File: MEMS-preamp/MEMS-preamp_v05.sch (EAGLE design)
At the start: 20 parts

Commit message: new mems preamp added
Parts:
- removed R2, R4: 200K, adafruit:TRIMPOT3386
- added POT1: POT-DUAL-PTV112-4420, CMU-ArtFab:POT-DUAL-PTV112-4420
- R1, R3: value 1K -> 220
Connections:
- net GROU[: now also POT1/2.E; no longer R4.A
- net N$10: now also POT1/2.A; no longer R4.S
- net N$5: now also POT1/1.E; no longer R2.A
- net N$9: now also POT1/1.A; no longer R2.S
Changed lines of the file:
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@@
 <layer number="132" name="bAdjust" color="7" fill="1" visible="yes" active="yes"/>
 <layer number="144" name="Drill_legend" color="7" fill="1" visible="yes" active="yes"/>
+<layer number="145" name="DrillLegend_01-16" color="7" fill="1" visible="yes" active="yes"/>
+<layer number="146" name="DrillLegend_01-20" color="7" fill="1" visible="yes" active="yes"/>
 <layer number="150" name="Notes" color="7" fill="1" visible="yes" active="yes"/>
 <layer number="151" name="HeatSink" color="7" fill="1" visible="yes" active="yes"/>
@@
 <attribute name="CON5" value="DC"/>
 </part>
-<part name="R1" library="CMU-ArtFab" deviceset="R-US_" device="0204/5" value="1K"/>
+<part name="R1" library="CMU-ArtFab" deviceset="R-US_" device="0204/5" value="220"/>
 <part name="GND2" library="supply1" deviceset="GND" device=""/>
 <part name="R9" library="CMU-ArtFab" deviceset="R-US_" device="0204/5" value="10"/>
@@
 <part name="GND1" library="supply1" deviceset="GND" device=""/>
 <part name="R10" library="CMU-ArtFab" deviceset="R-US_" device="0204/5" value="390"/>
-<part name="R2" library="adafruit" deviceset="TRIMPOT" device="3386" value="200K"/>
 <part name="J_REG_12V" library="CMU-ArtFab" deviceset="POLOLU_VOLTAGE_REGULATORS_3PIN" device="" value="POLOLU_VOLTAGE_REGULATORS_3PIN"/>
 <part name="GND12" library="supply1" deviceset="GND" device=""/>
@@
 <part name="P+2" library="supply1" deviceset="+12V" device=""/>
 <part name="BATTERY" library="SparkFun-Connectors" deviceset="CONN_02" device="LOCK"/>
-<part name="R3" library="CMU-ArtFab" deviceset="R-US_" device="0204/5" value="1K"/>
-<part name="R4" library="adafruit" deviceset="TRIMPOT" device="3386" value="200K"/>
+<part name="R3" library="CMU-ArtFab" deviceset="R-US_" device="0204/5" value="220"/>
 <part name="C2" library="rcl" deviceset="CPOL-EU" device="E2.5-5" value="10u"/>
+<part name="POT1" library="CMU-ArtFab" deviceset="POT-DUAL-PTV112" device="-4420"/>
 </parts>
 <sheets>
@@
 </instance>
 <instance part="R10" gate="G$1" x="142.24" y="162.56" rot="R90"/>
-<instance part="R2" gate="G$1" x="78.74" y="50.8" rot="R270"/>
 <instance part="J_REG_12V" gate="J_REG_5V" x="76.2" y="165.1"/>
 <instance part="GND12" gate="1" x="76.2" y="144.78" smashed="yes">
@@
 <instance part="BATTERY" gate="G$1" x="30.48" y="162.56" rot="R180"/>
 <instance part="R3" gate="G$1" x="119.38" y="71.12"/>
-<instance part="R4" gate="G$1" x="144.78" y="50.8" rot="R270"/>
 <instance part="C2" gate="G$1" x="165.1" y="71.12" smashed="yes" rot="R90">
 <attribute name="NAME" x="163.703" y="74.1426" size="1.778" layer="95" ratio="12"/>
 <attribute name="VALUE" x="163.703" y="66.5226" size="1.778" layer="96" ratio="12"/>
 </instance>
+<instance part="POT1" gate="/1" x="81.28" y="50.8" rot="R90"/>
+<instance part="POT1" gate="/2" x="147.32" y="53.34" rot="R90"/>
 </instances>
 <busses>
@@
 <wire x1="53.34" y1="50.8" x2="53.34" y2="68.58" width="0.1524" layer="91"/>
 <junction x="53.34" y="68.58"/>
-<pinref part="R2" gate="G$1" pin="A"/>
+<pinref part="POT1" gate="/1" pin="E"/>
 </segment>
 </net>
@@
 <pinref part="C1" gate="G$1" pin="+"/>
 <wire x1="76.2" y1="71.12" x2="88.9" y2="71.12" width="0.1524" layer="91"/>
-<pinref part="R2" gate="G$1" pin="S"/>
+<pinref part="POT1" gate="/1" pin="A"/>
 <wire x1="88.9" y1="71.12" x2="96.52" y2="71.12" width="0.1524" layer="91"/>
-<wire x1="78.74" y1="45.72" x2="78.74" y2="40.64" width="0.1524" layer="91"/>
-<wire x1="78.74" y1="40.64" x2="88.9" y2="40.64" width="0.1524" layer="91"/>
-<wire x1="88.9" y1="40.64" x2="88.9" y2="71.12" width="0.1524" layer="91"/>
+<wire x1="88.9" y1="50.8" x2="88.9" y2="71.12" width="0.1524" layer="91"/>
 <junction x="88.9" y="71.12"/>
 </segment>
@@
 <segment>
 <pinref part="OPA2134" gate="B" pin="OUT"/>
-<wire x1="152.4" y1="71.12" x2="154.94" y2="71.12" width="0.1524" layer="91"/>
-<wire x1="154.94" y1="71.12" x2="154.94" y2="40.64" width="0.1524" layer="91"/>
-<wire x1="154.94" y1="40.64" x2="144.78" y2="40.64" width="0.1524" layer="91"/>
-<pinref part="R4" gate="G$1" pin="S"/>
-<wire x1="144.78" y1="40.64" x2="144.78" y2="45.72" width="0.1524" layer="91"/>
 <pinref part="C2" gate="G$1" pin="+"/>
 <wire x1="162.56" y1="71.12" x2="154.94" y2="71.12" width="0.1524" layer="91"/>
+<pinref part="POT1" gate="/2" pin="A"/>
+<wire x1="154.94" y1="71.12" x2="152.4" y2="71.12" width="0.1524" layer="91"/>
+<wire x1="154.94" y1="53.34" x2="154.94" y2="71.12" width="0.1524" layer="91"/>
 <junction x="154.94" y="71.12"/>
 </segment>
@@
 <pinref part="OPA2134" gate="B" pin="-IN"/>
 <wire x1="129.54" y1="68.58" x2="134.62" y2="68.58" width="0.1524" layer="91"/>
-<pinref part="R4" gate="G$1" pin="A"/>
 <wire x1="134.62" y1="68.58" x2="137.16" y2="68.58" width="0.1524" layer="91"/>
-<wire x1="139.7" y1="50.8" x2="139.7" y2="53.34" width="0.1524" layer="91"/>
 <wire x1="139.7" y1="53.34" x2="134.62" y2="53.34" width="0.1524" layer="91"/>
 <wire x1="134.62" y1="53.34" x2="134.62" y2="68.58" width="0.1524" layer="91"/>
 <junction x="134.62" y="68.58"/>
-</segment>
-</net>
+<pinref part="POT1" gate="/2" pin="E"/>
+</segment>
+</net>

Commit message: new mems preamp added
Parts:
- POT1: value POT-DUAL-PTV112-4420 -> 50k
- R1, R3: value 220 -> 1k
- R7, R8: value 47K -> 150k
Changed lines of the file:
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@@
 <part name="GND8" library="supply1" deviceset="GND" device=""/>
 <part name="GND4" library="supply1" deviceset="GND" device=""/>
-<part name="R7" library="CMU-ArtFab" deviceset="R-US_" device="0204/5" value="47K"/>
+<part name="R7" library="CMU-ArtFab" deviceset="R-US_" device="0204/5" value="150k"/>
 <part name="OPA2134" library="linear" deviceset="OPA2*" device="PA" technology="134" value="OPA2134PA">
 <attribute name="IC_NAME" value="TL072"/>
@@
 <attribute name="CON5" value="DC"/>
 </part>
-<part name="R1" library="CMU-ArtFab" deviceset="R-US_" device="0204/5" value="220"/>
+<part name="R1" library="CMU-ArtFab" deviceset="R-US_" device="0204/5" value="1k"/>
 <part name="GND2" library="supply1" deviceset="GND" device=""/>
 <part name="R9" library="CMU-ArtFab" deviceset="R-US_" device="0204/5" value="10"/>
 <part name="C4" library="rcl" deviceset="CPOL-EU" device="E2.5-5" value="100u"/>
-<part name="R8" library="CMU-ArtFab" deviceset="R-US_" device="0204/5" value="47K"/>
+<part name="R8" library="CMU-ArtFab" deviceset="R-US_" device="0204/5" value="150k"/>
 <part name="U$1" library="CMU-ArtFab" deviceset="1/8&quot;-F-STEREO-PCB" device=""/>
 <part name="GND10" library="supply1" deviceset="GND" device=""/>
@@
 <part name="P+2" library="supply1" deviceset="+12V" device=""/>
 <part name="BATTERY" library="SparkFun-Connectors" deviceset="CONN_02" device="LOCK"/>
-<part name="R3" library="CMU-ArtFab" deviceset="R-US_" device="0204/5" value="220"/>
+<part name="R3" library="CMU-ArtFab" deviceset="R-US_" device="0204/5" value="1k"/>
 <part name="C2" library="rcl" deviceset="CPOL-EU" device="E2.5-5" value="10u"/>
-<part name="POT1" library="CMU-ArtFab" deviceset="POT-DUAL-PTV112" device="-4420"/>
+<part name="POT1" library="CMU-ArtFab" deviceset="POT-DUAL-PTV112" device="-4420" value="50k"/>
 </parts>
 <sheets>

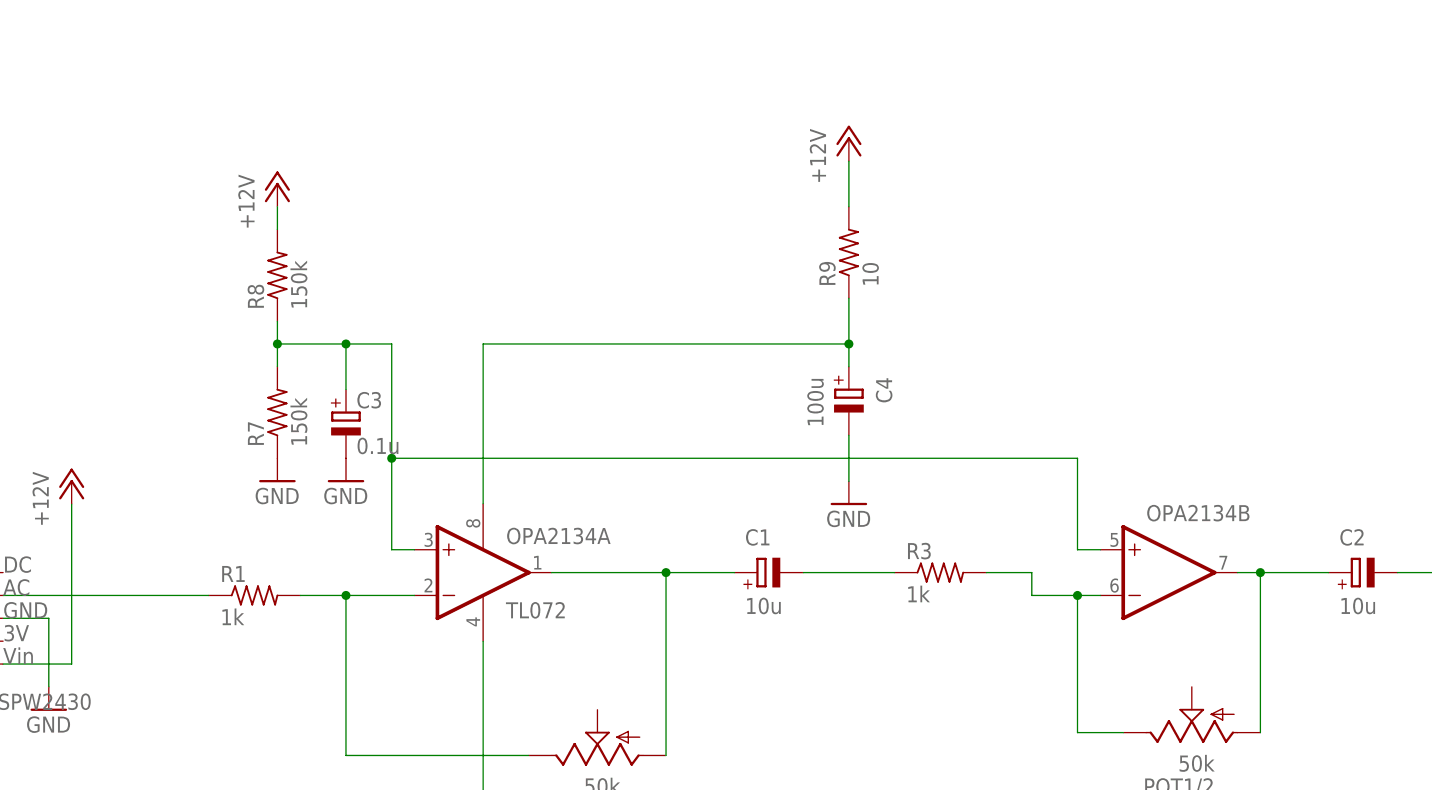
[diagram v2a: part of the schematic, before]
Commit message: new design for piezo premamp piezo-preamp-tickler_V3-2_single-supply-OPA1642 added
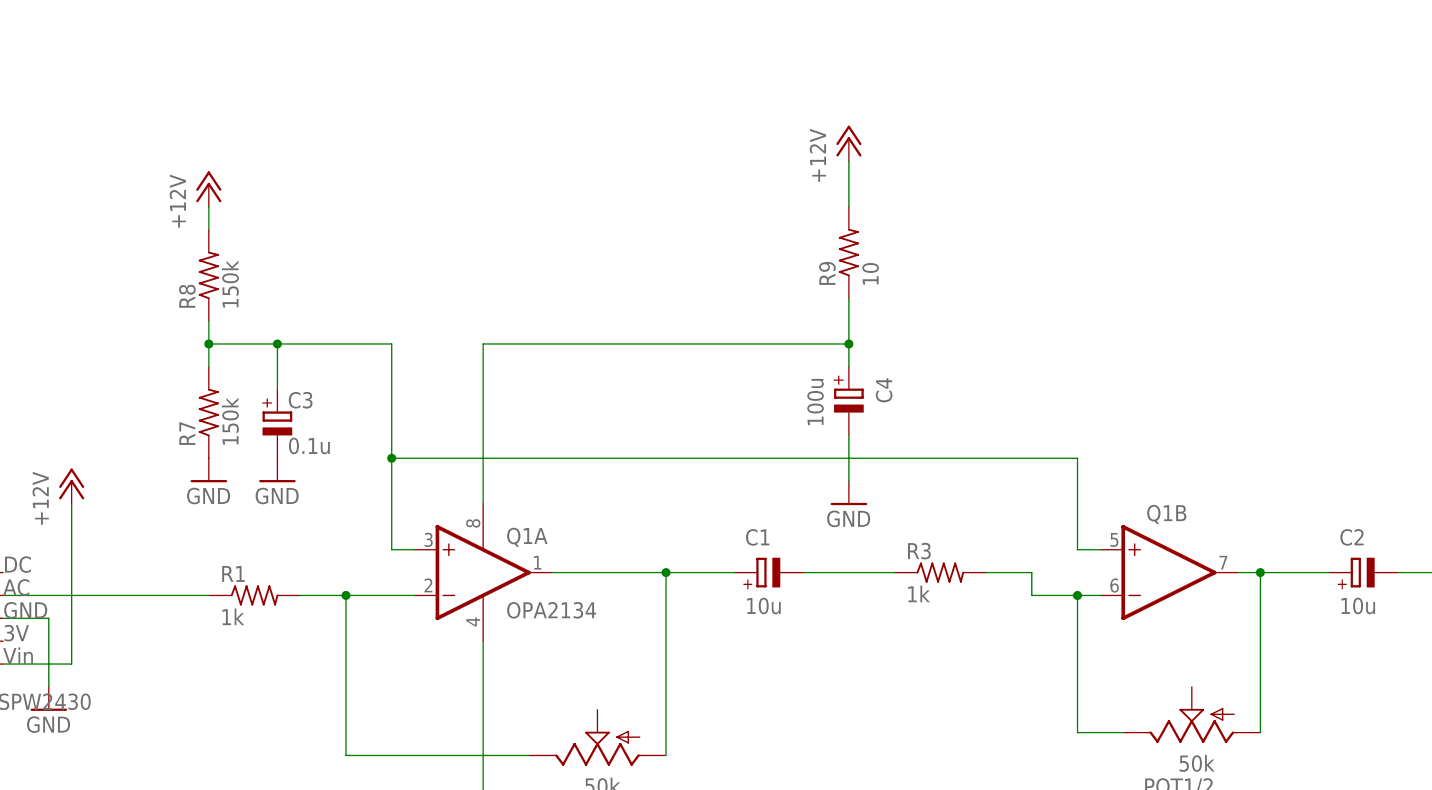
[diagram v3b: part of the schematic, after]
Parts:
- Q1: value OPA2134PA -> OPA2134; IC_NAME TL072 -> OPA2134
- renumbered OPA2134 to Q1
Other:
- moved on the sheet: C3, R7, R8
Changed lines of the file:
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@@
 <part name="GND4" library="supply1" deviceset="GND" device=""/>
 <part name="R7" library="CMU-ArtFab" deviceset="R-US_" device="0204/5" value="150k"/>
-<part name="OPA2134" library="linear" deviceset="OPA2*" device="PA" technology="134" value="OPA2134PA">
-<attribute name="IC_NAME" value="TL072"/>
+<part name="Q1" library="linear" deviceset="OPA2*" device="PA" technology="134" value="OPA2134">
+<attribute name="IC_NAME" value="OPA2134"/>
 </part>
 <part name="JP1" library="SparkFun-Connectors" deviceset="M05" device="LOCK" value="Adafruit-SPW2430">
@@
 </plain>
 <instances>
-<instance part="C3" gate="G$1" x="53.34" y="88.9" smashed="yes">
-<attribute name="NAME" x="54.483" y="89.3826" size="1.778" layer="95" ratio="12"/>
-<attribute name="VALUE" x="54.483" y="84.3026" size="1.778" layer="96" ratio="12"/>
+<instance part="C3" gate="G$1" x="45.72" y="88.9" smashed="yes">
+<attribute name="NAME" x="46.863" y="89.3826" size="1.778" layer="95" ratio="12"/>
+<attribute name="VALUE" x="46.863" y="84.3026" size="1.778" layer="96" ratio="12"/>
 </instance>
 <instance part="C1" gate="G$1" x="99.06" y="71.12" smashed="yes" rot="R90">
@@
 <attribute name="VALUE" x="97.663" y="66.5226" size="1.778" layer="96" ratio="12"/>
 </instance>
-<instance part="GND3" gate="1" x="45.72" y="81.28" smashed="yes">
+<instance part="GND3" gate="1" x="38.1" y="81.28" smashed="yes">
+<attribute name="VALUE" x="35.56" y="78.74" size="1.778" layer="96" ratio="12"/>
+</instance>
+<instance part="GND5" gate="1" x="45.72" y="81.28" smashed="yes">
 <attribute name="VALUE" x="43.18" y="78.74" size="1.778" layer="96" ratio="12"/>
-</instance>
-<instance part="GND5" gate="1" x="53.34" y="81.28" smashed="yes">
-<attribute name="VALUE" x="50.8" y="78.74" size="1.778" layer="96" ratio="12"/>
 </instance>
 <instance part="GND8" gate="1" x="109.22" y="78.74" smashed="yes">
@@
 <attribute name="VALUE" x="66.04" y="40.64" size="1.778" layer="96" ratio="12"/>
 </instance>
-<instance part="R7" gate="G$1" x="45.72" y="88.9" rot="R90"/>
-<instance part="OPA2134" gate="A" x="68.58" y="71.12" smashed="yes">
+<instance part="R7" gate="G$1" x="38.1" y="88.9" rot="R90"/>
+<instance part="Q1" gate="A" x="68.58" y="71.12" smashed="yes">
 <attribute name="NAME" x="71.12" y="74.295" size="1.778" layer="95"/>
 <attribute name="IC_NAME" x="71.12" y="66.04" size="1.778" layer="96"/>
 </instance>
-<instance part="OPA2134" gate="B" x="144.78" y="71.12" smashed="yes">
+<instance part="Q1" gate="B" x="144.78" y="71.12" smashed="yes">
 <attribute name="NAME" x="142.24" y="76.835" size="1.778" layer="95"/>
 </instance>
@@
 <attribute name="VALUE" x="104.6226" y="92.837" size="1.778" layer="96" ratio="12" rot="R270"/>
 </instance>
-<instance part="R8" gate="G$1" x="45.72" y="104.14" rot="R90"/>
+<instance part="R8" gate="G$1" x="38.1" y="104.14" rot="R90"/>
 <instance part="U$1" gate="G$1" x="195.58" y="63.5"/>
 <instance part="GND10" gate="1" x="185.42" y="60.96" smashed="yes">
@@
 <attribute name="VALUE" x="2.54" y="147.32" size="1.778" layer="96" ratio="12"/>
 </instance>
-<instance part="P+6" gate="1" x="45.72" y="114.3"/>
+<instance part="P+6" gate="1" x="38.1" y="114.3"/>
 <instance part="POWER" gate="G$1" x="12.7" y="157.48"/>
 <instance part="P+2" gate="1" x="22.86" y="81.28"/>
@@
 <pinref part="GND4" gate="1" pin="GND"/>
 <wire x1="68.58" y1="45.72" x2="68.58" y2="63.5" width="0.1524" layer="91"/>
-<pinref part="OPA2134" gate="A" pin="V-"/>
+<pinref part="Q1" gate="A" pin="V-"/>
 </segment>
 <segment>
@@
 <net name="N$8" class="0">
 <segment>
-<wire x1="53.34" y1="96.52" x2="53.34" y2="91.44" width="0.1524" layer="91"/>
+<wire x1="45.72" y1="96.52" x2="45.72" y2="91.44" width="0.1524" layer="91"/>
 <pinref part="C3" gate="G$1" pin="+"/>
-<wire x1="53.34" y1="96.52" x2="58.42" y2="96.52" width="0.1524" layer="91"/>
+<wire x1="45.72" y1="96.52" x2="58.42" y2="96.52" width="0.1524" layer="91"/>
 <wire x1="58.42" y1="96.52" x2="58.42" y2="83.82" width="0.1524" layer="91"/>
-<pinref part="OPA2134" gate="A" pin="+IN"/>
+<pinref part="Q1" gate="A" pin="+IN"/>
 <wire x1="58.42" y1="83.82" x2="58.42" y2="73.66" width="0.1524" layer="91"/>
 <wire x1="58.42" y1="73.66" x2="60.96" y2="73.66" width="0.1524" layer="91"/>
 <pinref part="R7" gate="G$1" pin="2"/>
 <pinref part="R8" gate="G$1" pin="1"/>
-<wire x1="45.72" y1="99.06" x2="45.72" y2="96.52" width="0.1524" layer="91"/>
-<wire x1="45.72" y1="96.52" x2="45.72" y2="93.98" width="0.1524" layer="91"/>
-<wire x1="53.34" y1="96.52" x2="45.72" y2="96.52" width="0.1524" layer="91"/>
-<junction x="53.34" y="96.52"/>
+<wire x1="38.1" y1="99.06" x2="38.1" y2="96.52" width="0.1524" layer="91"/>
+<wire x1="38.1" y1="96.52" x2="38.1" y2="93.98" width="0.1524" layer="91"/>
+<wire x1="45.72" y1="96.52" x2="38.1" y2="96.52" width="0.1524" layer="91"/>
 <junction x="45.72" y="96.52"/>
-<pinref part="OPA2134" gate="B" pin="+IN"/>
+<junction x="38.1" y="96.52"/>
+<pinref part="Q1" gate="B" pin="+IN"/>
 <wire x1="137.16" y1="73.66" x2="134.62" y2="73.66" width="0.1524" layer="91"/>
 <wire x1="134.62" y1="73.66" x2="134.62" y2="83.82" width="0.1524" layer="91"/>
@@
 <wire x1="53.34" y1="50.8" x2="73.66" y2="50.8" width="0.1524" layer="91"/>
 <pinref part="R1" gate="G$1" pin="2"/>
-<pinref part="OPA2134" gate="A" pin="-IN"/>
+<pinref part="Q1" gate="A" pin="-IN"/>
 <wire x1="48.26" y1="68.58" x2="53.34" y2="68.58" width="0.1524" layer="91"/>
 <wire x1="53.34" y1="68.58" x2="60.96" y2="68.58" width="0.1524" layer="91"/>
@@
 <net name="N$9" class="0">
 <segment>
-<pinref part="OPA2134" gate="A" pin="OUT"/>
+<pinref part="Q1" gate="A" pin="OUT"/>
 <pinref part="C1" gate="G$1" pin="+"/>
 <wire x1="76.2" y1="71.12" x2="88.9" y2="71.12" width="0.1524" layer="91"/>
@@
 <pinref part="R9" gate="G$1" pin="1"/>
 <wire x1="109.22" y1="101.6" x2="109.22" y2="96.52" width="0.1524" layer="91"/>
-<pinref part="OPA2134" gate="A" pin="V+"/>
+<pinref part="Q1" gate="A" pin="V+"/>
 <wire x1="109.22" y1="96.52" x2="109.22" y2="93.98" width="0.1524" layer="91"/>
 <wire x1="109.22" y1="96.52" x2="68.58" y2="96.52" width="0.1524" layer="91"/>
@@
 <segment>
 <pinref part="R8" gate="G$1" pin="2"/>
-<wire x1="45.72" y1="111.76" x2="45.72" y2="109.22" width="0.1524" layer="91"/>
+<wire x1="38.1" y1="111.76" x2="38.1" y2="109.22" width="0.1524" layer="91"/>
 <pinref part="P+6" gate="1" pin="+12V"/>
 </segment>
@@
 <net name="N$10" class="0">
 <segment>
-<pinref part="OPA2134" gate="B" pin="OUT"/>
+<pinref part="Q1" gate="B" pin="OUT"/>
 <pinref part="C2" gate="G$1" pin="+"/>
 <wire x1="162.56" y1="71.12" x2="154.94" y2="71.12" width="0.1524" layer="91"/>
@@
 <wire x1="124.46" y1="71.12" x2="129.54" y2="71.12" width="0.1524" layer="91"/>
 <wire x1="129.54" y1="71.12" x2="129.54" y2="68.58" width="0.1524" layer="91"/>
-<pinref part="OPA2134" gate="B" pin="-IN"/>
+<pinref part="Q1" gate="B" pin="-IN"/>
 <wire x1="129.54" y1="68.58" x2="134.62" y2="68.58" width="0.1524" layer="91"/>
 <wire x1="134.62" y1="68.58" x2="137.16" y2="68.58" width="0.1524" layer="91"/>
